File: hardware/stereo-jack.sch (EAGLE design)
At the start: 4 parts

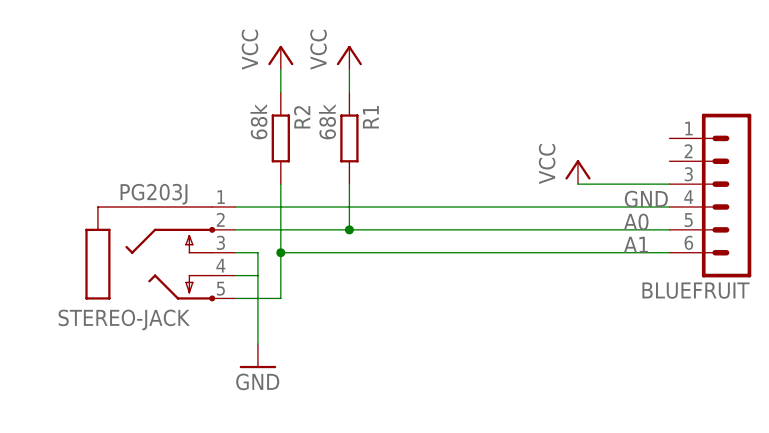
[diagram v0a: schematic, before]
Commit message: simplify board schematic and add layout
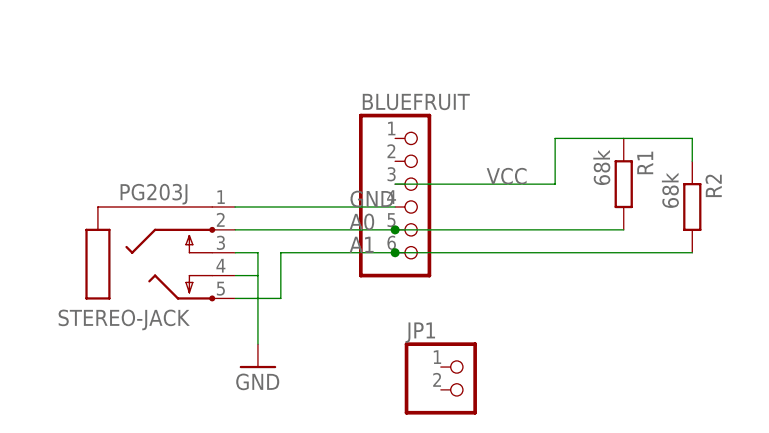
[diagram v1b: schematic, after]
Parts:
- added JP1: (no value), pinhead:PINHD-1X2
- BLUEFRUIT: device con-lstb:MA06-1 -> pinhead:PINHD-1X6
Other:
- moved on the sheet: R1, R2
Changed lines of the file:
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@@
 <parts>
 <part name="STEREO-JACK" library="con-hirschmann" library_urn="urn:adsk.eagle:library:153" deviceset="PG203J" device="" package3d_urn="urn:adsk.eagle:package:7447/1"/>
-<part name="P+1" library="supply1" library_urn="urn:adsk.eagle:library:371" deviceset="VCC" device=""/>
 <part name="R1" library="resistor" library_urn="urn:adsk.eagle:library:348" deviceset="R-EU_" device="0207/7" package3d_urn="urn:adsk.eagle:package:25942/1" value="68k"/>
 <part name="R2" library="resistor" library_urn="urn:adsk.eagle:library:348" deviceset="R-EU_" device="0207/7" package3d_urn="urn:adsk.eagle:package:25942/1" value="68k"/>
-<part name="P+2" library="supply1" library_urn="urn:adsk.eagle:library:371" deviceset="VCC" device=""/>
-<part name="P+3" library="supply1" library_urn="urn:adsk.eagle:library:371" deviceset="VCC" device=""/>
 <part name="GND1" library="supply1" library_urn="urn:adsk.eagle:library:371" deviceset="GND" device=""/>
-<part name="BLUEFRUIT" library="con-lstb" library_urn="urn:adsk.eagle:library:162" deviceset="MA06-1" device="" package3d_urn="urn:adsk.eagle:package:8340/1"/>
+<part name="JP1" library="pinhead" library_urn="urn:adsk.eagle:library:325" deviceset="PINHD-1X2" device="" package3d_urn="urn:adsk.eagle:package:22435/2"/>
+<part name="BLUEFRUIT" library="pinhead" library_urn="urn:adsk.eagle:library:325" deviceset="PINHD-1X6" device="" package3d_urn="urn:adsk.eagle:package:22472/2"/>
 </parts>
 <sheets>
@@
 <instances>
 <instance part="STEREO-JACK" gate="1" x="0" y="22.86" rot="R180"/>
-<instance part="P+1" gate="VCC" x="50.8" y="35.56"/>
-<instance part="R1" gate="G$1" x="25.4" y="38.1" rot="R270"/>
-<instance part="R2" gate="G$1" x="17.78" y="38.1" rot="R270"/>
-<instance part="P+2" gate="VCC" x="25.4" y="48.26"/>
-<instance part="P+3" gate="VCC" x="17.78" y="48.26"/>
+<instance part="R1" gate="G$1" x="55.88" y="33.02" rot="R270"/>
+<instance part="R2" gate="G$1" x="63.5" y="30.48" rot="R270"/>
 <instance part="GND1" gate="1" x="15.24" y="12.7"/>
-<instance part="BLUEFRUIT" gate="1" x="68.58" y="30.48" rot="R180"/>
+<instance part="JP1" gate="G$1" x="38.1" y="10.16"/>
+<instance part="BLUEFRUIT" gate="A" x="33.02" y="30.48"/>
 </instances>
 <busses>
 </busses>
 <nets>
-<net name="VCC" class="0">
-<segment>
-<pinref part="P+1" gate="VCC" pin="VCC"/>
-<wire x1="60.96" y1="33.02" x2="50.8" y2="33.02" width="0.1524" layer="91"/>
-<pinref part="BLUEFRUIT" gate="1" pin="3"/>
-</segment>
-<segment>
-<pinref part="R2" gate="G$1" pin="1"/>
-<pinref part="P+3" gate="VCC" pin="VCC"/>
-<wire x1="17.78" y1="43.18" x2="17.78" y2="45.72" width="0.1524" layer="91"/>
-</segment>
-<segment>
-<pinref part="R1" gate="G$1" pin="1"/>
-<pinref part="P+2" gate="VCC" pin="VCC"/>
-<wire x1="25.4" y1="43.18" x2="25.4" y2="45.72" width="0.1524" layer="91"/>
-</segment>
-</net>
 <net name="GND" class="0">
 <segment>
 <pinref part="STEREO-JACK" gate="1" pin="1"/>
-<label x="55.88" y="30.48" size="1.778" layer="95"/>
-<wire x1="60.96" y1="30.48" x2="12.7" y2="30.48" width="0.1524" layer="91"/>
-<pinref part="BLUEFRUIT" gate="1" pin="4"/>
+<label x="25.4" y="30.48" size="1.778" layer="95"/>
+<wire x1="30.48" y1="30.48" x2="12.7" y2="30.48" width="0.1524" layer="91"/>
+<pinref part="BLUEFRUIT" gate="A" pin="4"/>
 </segment>
 <segment>
@@
 <net name="A1" class="0">
 <segment>
-<pinref part="R2" gate="G$1" pin="2"/>
 <wire x1="17.78" y1="20.32" x2="17.78" y2="25.4" width="0.1524" layer="91"/>
 <pinref part="STEREO-JACK" gate="1" pin="5"/>
-<wire x1="17.78" y1="25.4" x2="17.78" y2="33.02" width="0.1524" layer="91"/>
 <wire x1="12.7" y1="20.32" x2="17.78" y2="20.32" width="0.1524" layer="91"/>
-<wire x1="60.96" y1="25.4" x2="17.78" y2="25.4" width="0.1524" layer="91"/>
-<junction x="17.78" y="25.4"/>
-<pinref part="BLUEFRUIT" gate="1" pin="6"/>
-<label x="55.88" y="25.4" size="1.778" layer="95"/>
+<label x="25.4" y="25.4" size="1.778" layer="95"/>
+<pinref part="R2" gate="G$1" pin="2"/>
+<wire x1="17.78" y1="25.4" x2="30.48" y2="25.4" width="0.1524" layer="91"/>
+<pinref part="BLUEFRUIT" gate="A" pin="6"/>
+<wire x1="30.48" y1="25.4" x2="63.5" y2="25.4" width="0.1524" layer="91"/>
+<junction x="30.48" y="25.4"/>
 </segment>
 </net>
 <net name="A0" class="0">
 <segment>
-<wire x1="60.96" y1="27.94" x2="25.4" y2="27.94" width="0.1524" layer="91"/>
 <pinref part="STEREO-JACK" gate="1" pin="2"/>
+<label x="25.4" y="27.94" size="1.778" layer="95"/>
 <pinref part="R1" gate="G$1" pin="2"/>
-<wire x1="25.4" y1="27.94" x2="12.7" y2="27.94" width="0.1524" layer="91"/>
-<wire x1="25.4" y1="33.02" x2="25.4" y2="27.94" width="0.1524" layer="91"/>
-<junction x="25.4" y="27.94"/>
-<pinref part="BLUEFRUIT" gate="1" pin="5"/>
-<label x="55.88" y="27.94" size="1.778" layer="95"/>
+<wire x1="12.7" y1="27.94" x2="30.48" y2="27.94" width="0.1524" layer="91"/>
+<pinref part="BLUEFRUIT" gate="A" pin="5"/>
+<wire x1="30.48" y1="27.94" x2="55.88" y2="27.94" width="0.1524" layer="91"/>
+<junction x="30.48" y="27.94"/>
 </segment>
 </net>
+<net name="VCC" class="0">
+<segment>
+<pinref part="R2" gate="G$1" pin="1"/>
+<wire x1="63.5" y1="35.56" x2="63.5" y2="38.1" width="0.1524" layer="91"/>
+<pinref part="R1" gate="G$1" pin="1"/>
+<wire x1="63.5" y1="38.1" x2="55.88" y2="38.1" width="0.1524" layer="91"/>
+<wire x1="55.88" y1="38.1" x2="48.26" y2="38.1" width="0.1524" layer="91"/>
+<wire x1="48.26" y1="38.1" x2="48.26" y2="33.02" width="0.1524" layer="91"/>
+<wire x1="48.26" y1="33.02" x2="30.48" y2="33.02" width="0.1524" layer="91"/>
+<label x="40.64" y="33.02" size="1.778" layer="95"/>
+<pinref part="BLUEFRUIT" gate="A" pin="3"/>
+</segment>
+</net>
